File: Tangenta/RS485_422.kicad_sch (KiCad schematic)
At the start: 1 part, among them J14 RC01133

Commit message: ...
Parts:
- removed J14: RC01133, RJ45_SIMPLE:RJ45_SIMPLE, symbol RJ45_SIMPLE:RC01133
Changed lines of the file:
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@@
 (kicad_sch (version 20230121) (generator eeschema)
   (paper "A4")
-  (symbol (lib_id "RJ45_SIMPLE:RC01133") (at 103.505 68.58 0) (unit 1)
-    (in_bom yes) (on_board yes) (dnp no) (fields_autoplaced)
-    (property "Reference" "J14" (at 102.235 50.8 0)
-      (effects (font (size 1.27 1.27)))
-    )
-    (property "Value" "RC01133" (at 102.235 53.34 0)
-      (effects (font (size 1.27 1.27)))
-    )
-    (property "Footprint" "RJ45_SIMPLE:RJ45_SIMPLE" (at 104.775 93.98 0)
-      (effects (font (size 1.27 1.27) italic) hide)
-    )
-    (property "Datasheet" "https://atta.szlcsc.com/upload/public/pdf/source/20200728/C708616_F79F0C1A8A5D9701E7B7144C9F29FA5C.pdf" (at 92.075 96.52 0)
-      (effects (font (size 1.27 1.27)) (justify left) hide)
-    )
-    (property "LCSC" "C708616" (at 97.155 91.44 0)
-      (effects (font (size 1.27 1.27)) hide)
-    )
-    (pin "1")
-    (pin "10")
-    (pin "2")
-    (pin "3")
-    (pin "4")
-    (pin "5")
-    (pin "6")
-    (pin "7")
-    (pin "8")
-    (pin "9")
-    (instances
-      (project "Tangenta"
-        (path "/358d1bcf-7599-4352-8c4d-baa18a5f09e6/98e3b24f-9927-4339-b8fd-9deea91a522a"
-          (reference "J14") (unit 1)
-        )
-      )
-    )
-  )
 )

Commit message: UARTs schematic fanout.
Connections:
- no-connect marks 0 -> 8
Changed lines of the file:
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@@
 (kicad_sch (version 20230121) (generator eeschema)
   (paper "A4")
+  (no_connect (at 73.66 64.135))
+  (no_connect (at 73.66 48.895))
+  (no_connect (at 73.66 46.355))
+  (no_connect (at 73.66 51.435))
+  (no_connect (at 73.66 43.815))
+  (no_connect (at 73.66 69.215))
+  (no_connect (at 73.66 71.755))
+  (no_connect (at 73.66 66.675))
+  (bus_entry (at 54.61 71.755) (size 2.54 -2.54)
+    (stroke (width 0) (type default))
+  )
+  (bus_entry (at 54.61 74.295) (size 2.54 -2.54)
+    (stroke (width 0) (type default))
+  )
+  (bus_entry (at 54.61 69.215) (size 2.54 -2.54)
+    (stroke (width 0) (type default))
+  )
+  (bus_entry (at 54.61 48.895) (size 2.54 -2.54)
+    (stroke (width 0) (type default))
+  )
+  (bus_entry (at 54.61 46.355) (size 2.54 -2.54)
+    (stroke (width 0) (type default))
+  )
+  (bus_entry (at 54.61 51.435) (size 2.54 -2.54)
+    (stroke (width 0) (type default))
+  )
+  (bus_entry (at 54.61 66.675) (size 2.54 -2.54)
+    (stroke (width 0) (type default))
+  )
+  (bus_entry (at 54.61 53.975) (size 2.54 -2.54)
+    (stroke (width 0) (type default))
+  )
+  (bus (pts (xy 43.18 80.645) (xy 54.61 80.645))
+    (stroke (width 0) (type default))
+  )
+  (wire (pts (xy 26.67 34.925) (xy 38.1 34.925))
+    (stroke (width 0) (type default))
+  )
+  (wire (pts (xy 57.15 51.435) (xy 73.66 51.435))
+    (stroke (width 0) (type default))
+  )
+  (wire (pts (xy 26.67 31.115) (xy 38.1 31.115))
+    (stroke (width 0) (type default))
+  )
+  (wire (pts (xy 57.15 69.215) (xy 73.66 69.215))
+    (stroke (width 0) (type default))
+  )
+  (bus (pts (xy 54.61 46.355) (xy 54.61 48.895))
+    (stroke (width 0) (type default))
+  )
+  (wire (pts (xy 26.67 27.305) (xy 38.1 27.305))
+    (stroke (width 0) (type default))
+  )
+  (wire (pts (xy 26.67 23.495) (xy 38.1 23.495))
+    (stroke (width 0) (type default))
+  )
+  (bus (pts (xy 54.61 74.295) (xy 54.61 80.645))
+    (stroke (width 0) (type default))
+  )
+  (wire (pts (xy 57.15 66.675) (xy 73.66 66.675))
+    (stroke (width 0) (type default))
+  )
+  (wire (pts (xy 57.15 48.895) (xy 73.66 48.895))
+    (stroke (width 0) (type default))
+  )
+  (bus (pts (xy 54.61 69.215) (xy 54.61 71.755))
+    (stroke (width 0) (type default))
+  )
+  (bus (pts (xy 54.61 53.975) (xy 54.61 60.325))
+    (stroke (width 0) (type default))
+  )
+  (wire (pts (xy 57.15 71.755) (xy 73.66 71.755))
+    (stroke (width 0) (type default))
+  )
+  (bus (pts (xy 54.61 66.675) (xy 54.61 69.215))
+    (stroke (width 0) (type default))
+  )
+  (bus (pts (xy 54.61 71.755) (xy 54.61 74.295))
+    (stroke (width 0) (type default))
+  )
+  (bus (pts (xy 43.18 60.325) (xy 54.61 60.325))
+    (stroke (width 0) (type default))
+  )
+  (wire (pts (xy 57.15 46.355) (xy 73.66 46.355))
+    (stroke (width 0) (type default))
+  )
+  (wire (pts (xy 57.15 43.815) (xy 73.66 43.815))
+    (stroke (width 0) (type default))
+  )
+  (wire (pts (xy 57.15 64.135) (xy 73.66 64.135))
+    (stroke (width 0) (type default))
+  )
+  (bus (pts (xy 54.61 51.435) (xy 54.61 53.975))
+    (stroke (width 0) (type default))
+  )
+  (bus (pts (xy 54.61 48.895) (xy 54.61 51.435))
+    (stroke (width 0) (type default))
+  )
+  (label "GND" (at 29.21 23.495 0) (fields_autoplaced)
+    (effects (font (size 1.27 1.27)) (justify left bottom))
+  )
+  (label "UART_1.CTS" (at 73.66 51.435 180) (fields_autoplaced)
+    (effects (font (size 1.27 1.27)) (justify right bottom))
+  )
+  (label "3V3" (at 38.1 31.115 180) (fields_autoplaced)
+    (effects (font (size 1.27 1.27)) (justify right bottom))
+  )
+  (label "UART_2.CTS" (at 73.66 71.755 180) (fields_autoplaced)
+    (effects (font (size 1.27 1.27)) (justify right bottom))
+  )
+  (label "UART_2.TXD" (at 73.66 66.675 180) (fields_autoplaced)
+    (effects (font (size 1.27 1.27)) (justify right bottom))
+  )
+  (label "5V" (at 38.1 27.305 180) (fields_autoplaced)
+    (effects (font (size 1.27 1.27)) (justify right bottom))
+  )
+  (label "UART_2.RTS" (at 73.66 69.215 180) (fields_autoplaced)
+    (effects (font (size 1.27 1.27)) (justify right bottom))
+  )
+  (label "UART_2.RXD" (at 73.66 64.135 180) (fields_autoplaced)
+    (effects (font (size 1.27 1.27)) (justify right bottom))
+  )
+  (label "UART_1.RTS" (at 73.66 48.895 180) (fields_autoplaced)
+    (effects (font (size 1.27 1.27)) (justify right bottom))
+  )
+  (label "UART_1.TXD" (at 73.66 46.355 180) (fields_autoplaced)
+    (effects (font (size 1.27 1.27)) (justify right bottom))
+  )
+  (label "CHASSIS" (at 38.1 34.925 180) (fields_autoplaced)
+    (effects (font (size 1.27 1.27)) (justify right bottom))
+  )
+  (label "UART_1.RXD" (at 73.66 43.815 180) (fields_autoplaced)
+    (effects (font (size 1.27 1.27)) (justify right bottom))
+  )
+  (hierarchical_label "UART_1{RXD TXD RTS CTS}" (shape input) (at 43.18 60.325 180) (fields_autoplaced)
+    (effects (font (size 1.27 1.27)) (justify right))
+  )
+  (hierarchical_label "5V" (shape input) (at 26.67 27.305 180) (fields_autoplaced)
+    (effects (font (size 1.27 1.27)) (justify right))
+  )
+  (hierarchical_label "CHASSIS" (shape bidirectional) (at 26.67 34.925 180) (fields_autoplaced)
+    (effects (font (size 1.27 1.27)) (justify right))
+  )
+  (hierarchical_label "GND" (shape bidirectional) (at 26.67 23.495 180) (fields_autoplaced)
+    (effects (font (size 1.27 1.27)) (justify right))
+  )
+  (hierarchical_label "UART_2{RXD TXD RTS CTS}" (shape input) (at 43.18 80.645 180) (fields_autoplaced)
+    (effects (font (size 1.27 1.27)) (justify right))
+  )
+  (hierarchical_label "3V3" (shape input) (at 26.67 31.115 180) (fields_autoplaced)
+    (effects (font (size 1.27 1.27)) (justify right))
+  )
+  (symbol (lib_id "power:GNDREF") (at 38.1 23.495 90) (unit 1)
+    (in_bom yes) (on_board yes) (dnp no) (fields_autoplaced)
+    (property "Reference" "#PWR030" (at 44.45 23.495 0)
+      (effects (font (size 1.27 1.27)) hide)
+    )
+    (property "Value" "GNDREF" (at 43.18 23.495 0)
+      (effects (font (size 1.27 1.27)) hide)
+    )
+    (property "Footprint" "" (at 38.1 23.495 0)
+      (effects (font (size 1.27 1.27)) hide)
+    )
+    (property "Datasheet" "" (at 38.1 23.495 0)
+      (effects (font (size 1.27 1.27)) hide)
+    )
+    (pin "1")
+    (instances
+      (project "Tangenta"
+        (path "/358d1bcf-7599-4352-8c4d-baa18a5f09e6/b1871a4d-6a35-44e2-a9a2-9a4af684371d"
+          (reference "#PWR030") (unit 1)
+        )
+        (path "/358d1bcf-7599-4352-8c4d-baa18a5f09e6/f1c5822c-e7b8-40ae-bab0-71fd1c2cfc7c"
+          (reference "#PWR035") (unit 1)
+        )
+        (path "/358d1bcf-7599-4352-8c4d-baa18a5f09e6/98e3b24f-9927-4339-b8fd-9deea91a522a"
+          (reference "#PWR076") (unit 1)
+        )
+      )
+    )
+  )
 )

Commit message: ...
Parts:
- added C1 (x2): 100nF, Capacitor_SMD:C_0402_1005Metric, symbol Device:C_Small
- added C1 (x2): 10uF, Capacitor_SMD:C_0402_1005Metric, symbol Device:C_Small
- added Q3 (x8): BSS138, Package_TO_SOT_SMD:SOT-23, symbol Transistor_FET:BSS138
- added R2 (x8): 4.7k, Resistor_SMD:R_0402_1005Metric, symbol Device:R_Small_US
- added R2 (x2): 120R, Resistor_SMD:R_0402_1005Metric, symbol Device:R_Small_US
- added R2 (x4): 10R, Resistor_SMD:R_0402_1005Metric, symbol Device:R_Small_US
- added R2 (x8): 1.8k, Resistor_SMD:R_0402_1005Metric, symbol Device:R_Small_US
- added U19, U20: SN75HVD3082EDR, RS485_TRANS:RS485_TRANS, symbol RS485_TRANS:SN75HVD3082EDR
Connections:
- net 5V: now also C1.2, C1.2, C1.2, C1.2, R2.2, R2.2, R2.2, R2.2, R2.2, R2.2, R2.2, R2.2, U19.8 (VCC), U20.8 (VCC)
- net GNDREF: now also C1.1, C1.1, C1.1, C1.1, U19.5 (GND), U20.5 (GND)
- net UART_1.CTS: now also Q3.2 (S), R2.1
- net UART_1.RTS: now also Q3.2 (S), R2.1
- net UART_1.RXD: now also Q3.2 (S), R2.1
- net UART_1.TXD: now also Q3.2 (S), R2.1
- net UART_2.CTS: now also Q3.2 (S), R2.1
- net UART_2.RTS: now also Q3.2 (S), R2.1
- net UART_2.RXD: now also Q3.2 (S), R2.1
- net UART_2.TXD: now also Q3.2 (S), R2.1
- new net: R2.1, R2.2, U20.6 (A)
- new net: R2.2, R2.2, U20.7 (B)
- new net: R2.1, R2.2, U19.6 (A)
- new net: R2.2, R2.2, U19.7 (B)
- new net 1V8: Q3.1 (G), Q3.1 (G), Q3.1 (G), Q3.1 (G), Q3.1 (G), Q3.1 (G), Q3.1 (G), Q3.1 (G), R2.2, R2.2, R2.2, R2.2, R2.2, R2.2, R2.2, R2.2
- new net CTS_1_H: Q3.3 (D), R2.1, U19.3 (DE)
- new net CTS_2_H: Q3.3 (D), R2.1, U20.3 (DE)
- new net RS485_CH_1.A: R2.1
- new net RS485_CH_1.B: R2.1
- new net RS485_CH_2.A: R2.1
- new net RS485_CH_2.B: R2.1
- new net RTS_1_H: Q3.3 (D), R2.1, U19.2 (RE#)
- new net RTS_2_H: Q3.3 (D), R2.1, U20.2 (RE#)
- new net RXD_1_H: Q3.3 (D), R2.1, U19.1 (R)
- new net RXD_2_H: Q3.3 (D), R2.1, U20.1 (R)
- new net TXD_1_H: Q3.3 (D), R2.1, U19.4 (D)
- new net TXD_2_H: Q3.3 (D), R2.1, U20.4 (D)
- no-connect marks 8 -> 0

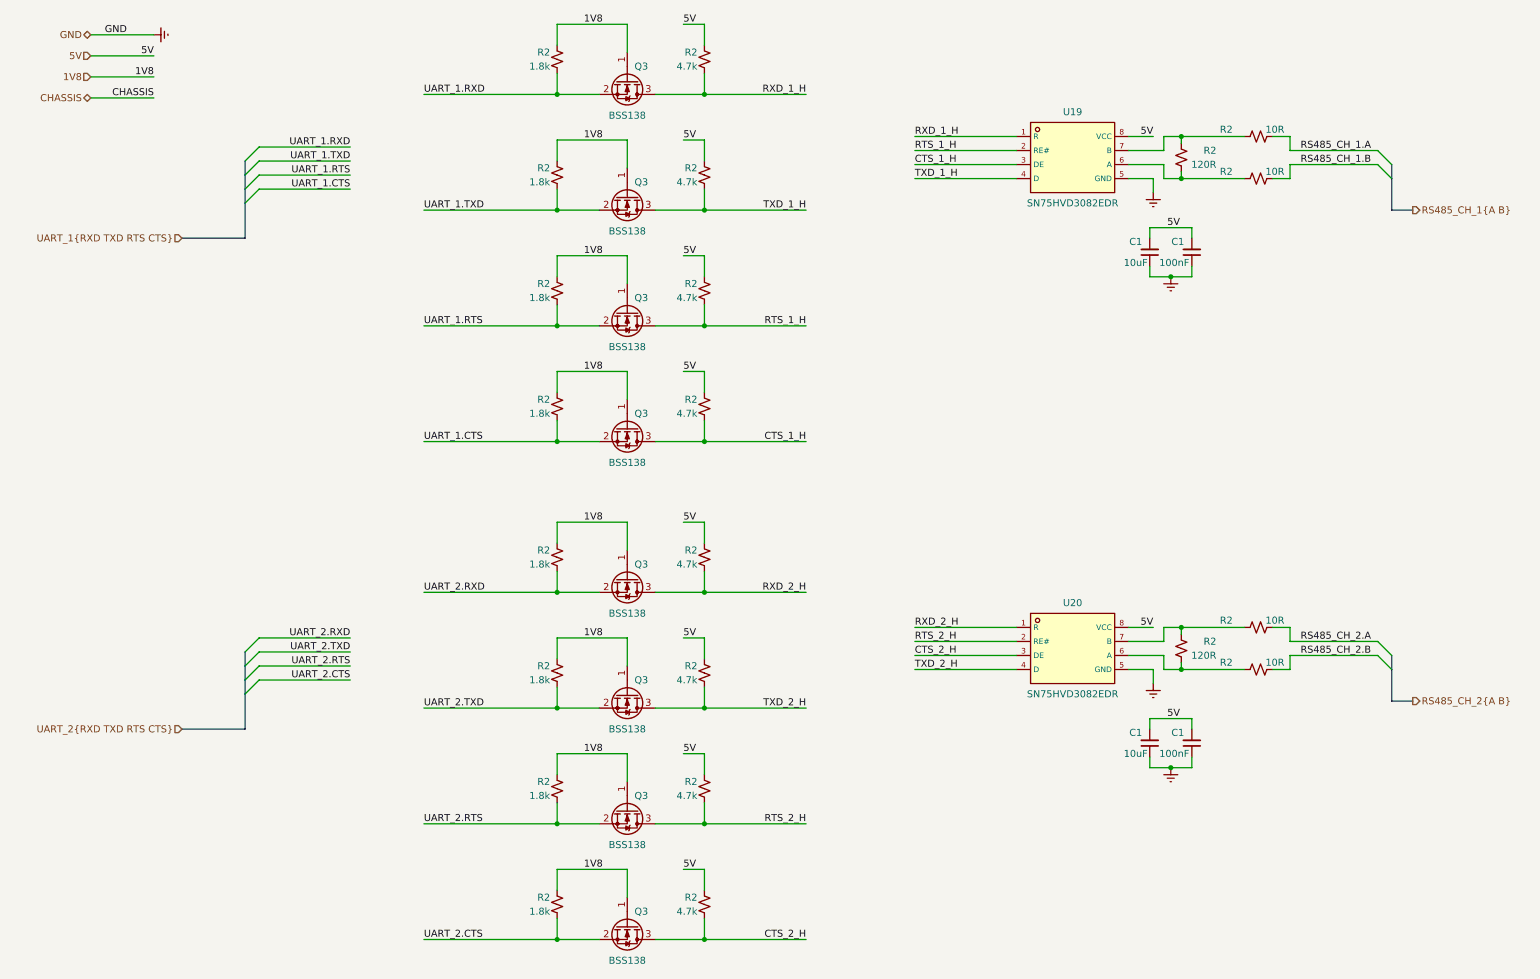
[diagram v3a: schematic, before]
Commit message: Dual RS485 routed, done.
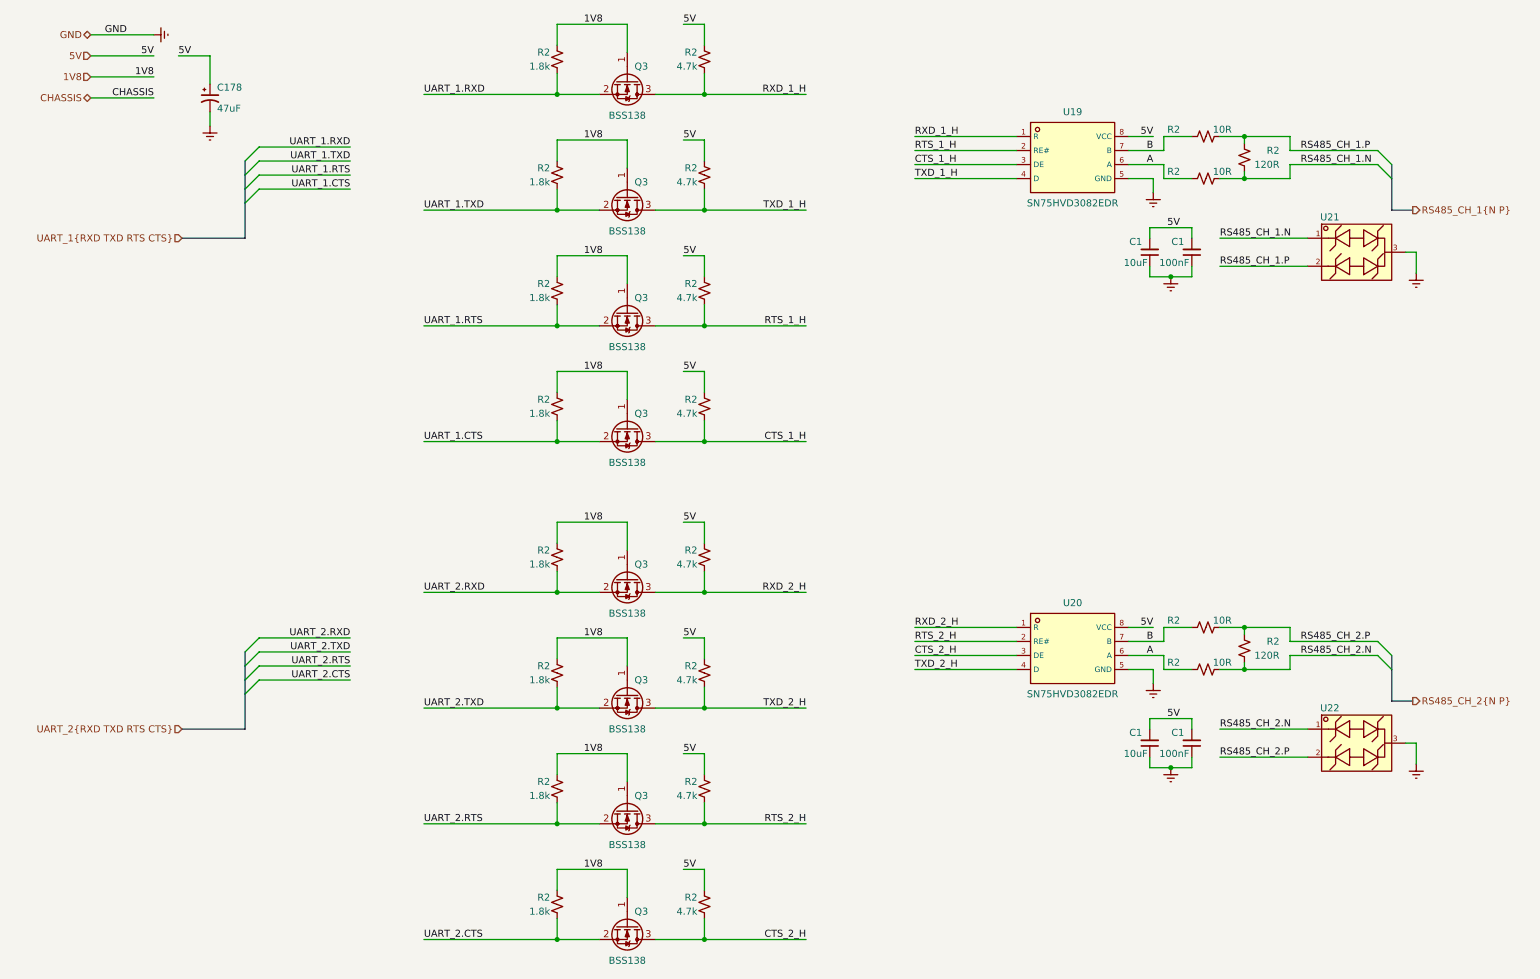
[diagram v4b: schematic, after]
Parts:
- added C178: 47uF, CAP_L5:CAP_L5, symbol CAP_L5:16CE47FSS
- added U21, U22: TPCDSOT23-SM712, ESD_RS485:ESD_RS485, symbol ESD_RS485:TPCDSOT23-SM712
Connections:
- net 5V: now also C178.1
- net GNDREF: now also C178.2, U21.3, U22.3
- net A: now reaches R2.2, U20.6 (A)
- net A: now also R2.2, U19.6 (A); no longer R2.1
- net B: now reaches R2.2, U20.7 (B)
- net B: now also R2.2, U19.7 (B); no longer R2.2
- net RS485_CH_1.A renamed RS485_CH_1.P
- net RS485_CH_1.P: now also R2.2, U21.2
- net RS485_CH_1.B renamed RS485_CH_1.N
- net RS485_CH_1.N: now also R2.1, U21.1
- net RS485_CH_2.A renamed RS485_CH_2.P
- net RS485_CH_2.P: now also R2.2, U22.2
- net RS485_CH_2.B renamed RS485_CH_2.N
- net RS485_CH_2.N: now also R2.1, U22.1
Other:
- moved on the sheet: R2
